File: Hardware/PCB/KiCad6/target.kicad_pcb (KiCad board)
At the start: 2 copper layers, 80 x 82 mm, 70 parts, among them J1 Additional Pins, J2 SW-5V, J3 SW-1, J4 SW-3.3V, J5 SW-2, J6 EXT_LED, J7 Conn_IN, J8 Conn_OUT, J9 USB_B_Micro, Q1 BSS138, Q2 BSS138, Q3 BSS138, Q4 BSS138, Q5 BC817, Q6 BC817, SW1 PROG, SW2 RST, U1 ESP32-WROOM-32D, U2 TSOP312xx, U3 AZ1117-3.3, U4 CH340C

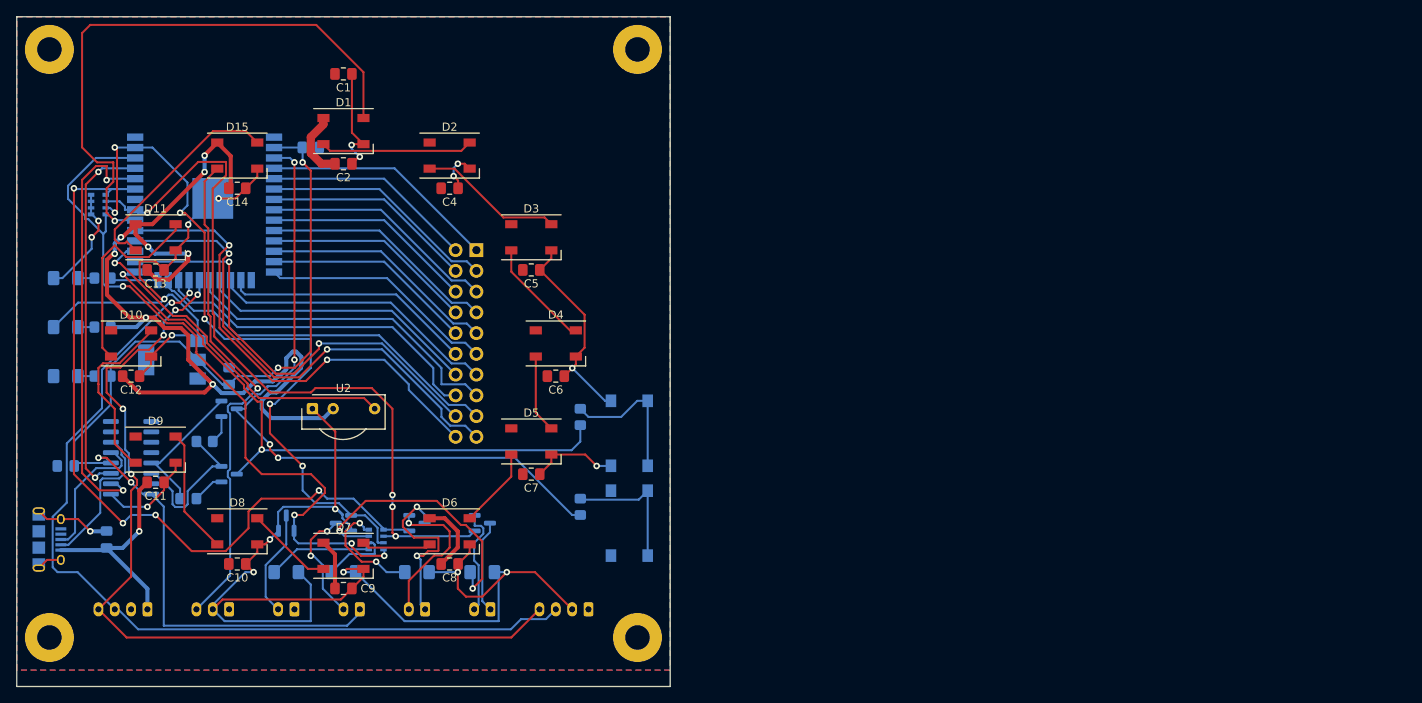
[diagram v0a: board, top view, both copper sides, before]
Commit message: PCB Update from current schema
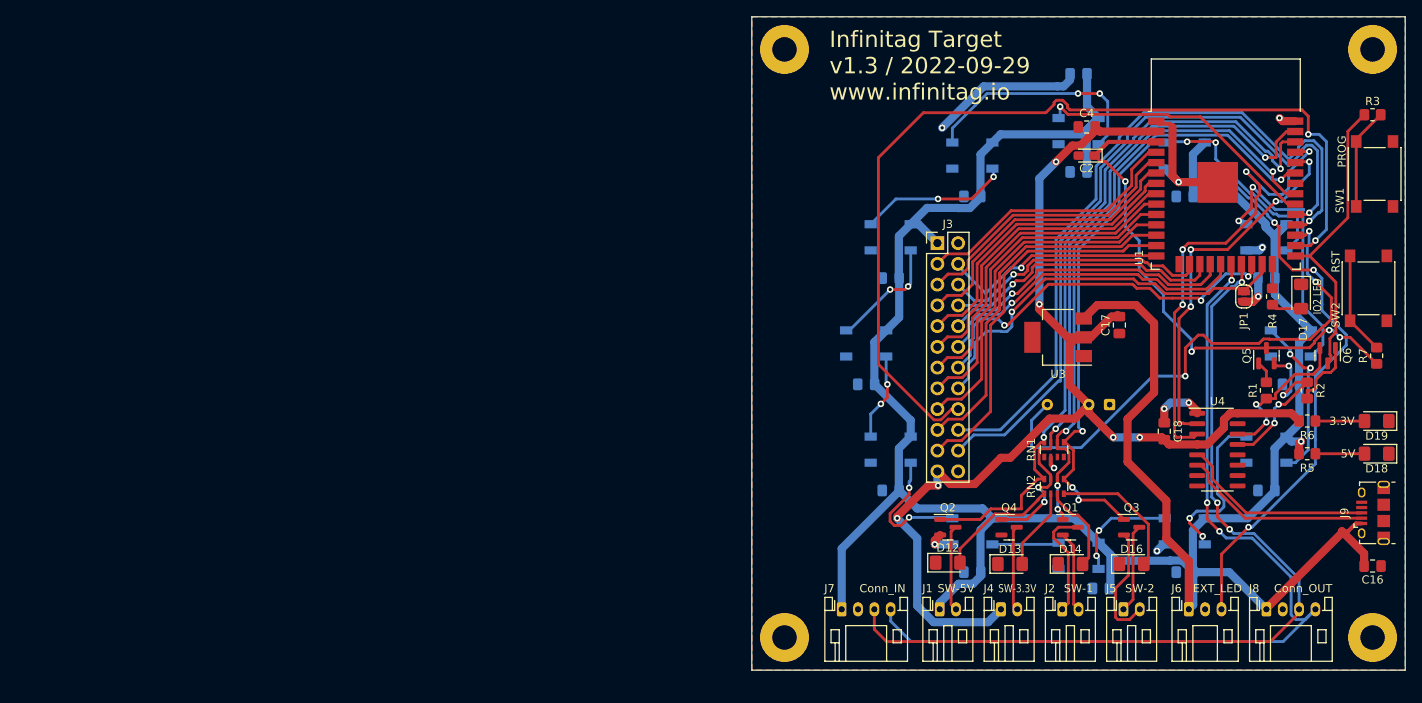
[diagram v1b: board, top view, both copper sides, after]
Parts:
- removed R9: 470, Resistor_SMD:R_0805_2012Metric_Pad1.20x1.40mm_HandSolder
- added C18: 100nF, Capacitor_SMD:C_0805_2012Metric_Pad1.18x1.45mm_HandSolder, F.Cu at (232.5, 100.8)
- added JP1: Disable ESP Log, Jumper:SolderJumper-2_P1.3mm_Open_RoundedPad1.0x1.5mm, F.Cu at (242.2, 84.2)
- added R3: 470, Resistor_SMD:R_0805_2012Metric_Pad1.20x1.40mm_HandSolder, F.Cu at (258.0, 62.0)
- C1: value 100uF -> 100nF; moved to B.Cu
- C10, C11, C12, C13, C14, C5, C6, C7, C8, C9, D1, D10, D11, D15, D2, D3, D4, D5, D6, D7, D8, D9, U2: moved to B.Cu
- C15: value 4.7uF -> 100nF
- C16: value 10uF -> 4.7uF; moved to F.Cu
- C17: value 100nF -> 10uF; moved to F.Cu
- C2: value 100nF -> 10uF; footprint Capacitor_SMD:C_0805_2012Metric_Pad1.18x1.45mm_HandSolder -> Capacitor_Tantalum_SMD:CP_EIA-2012-12_Kemet-R_Pad1.30x1.05mm_HandSolder
- D12, D13, D14, D16, D18, D19, J4, J5, J6, J7, J8, J9, Q1, Q2, Q3, Q4, Q5, Q6, R1, R2, R4, R7, RN1, RN2, SW1, SW2, U1, U3, U4: moved to F.Cu
- D17: value IO2 -> IO2 LED; moved to F.Cu
- J1: value Additional Pins -> SW-5V; footprint Connector_PinHeader_2.54mm:PinHeader_2x10_P2.54mm_Vertical -> Connector_JST:JST_PH_S2B-PH-K_1x02_P2.00mm_Horizontal; moved to F.Cu
- J2: value SW-5V -> SW-1; moved to F.Cu
- J3: value SW-1 -> Conn_02x12_Odd_Even; footprint Connector_JST:JST_PH_S2B-PH-K_1x02_P2.00mm_Horizontal -> Connector_PinHeader_2.54mm:PinHeader_2x12_P2.54mm_Vertical; moved to F.Cu
- R5: value 470 -> 1K; moved to F.Cu
- R6: value 1K -> 470; moved to F.Cu
- moved J9 162.1 mm to (258.1, 110.7)
- moved D18 161.2 mm to (258.5, 103.5), turned to 180 degrees
- moved D19 160.6 mm to (258.5, 99.5), turned to 180 degrees
- moved R7 156.0 mm to (258.5, 91.5), turned to 90 degrees
- moved D17 151.3 mm to (249.2, 84.2), turned to -90 degrees
- moved R5 149.0 mm to (250.0, 103.5), turned to 0 degrees
- moved R6 147.9 mm to (250.0, 99.5), turned to 0 degrees
- moved D10 142.0 mm to (248.0, 90.0), turned to 180 degrees
- moved C16 141.9 mm to (258.0, 117.2), turned to 180 degrees
- moved C12 139.7 mm to (245.0, 108.0), turned to 0 degrees
- moved C13 139.7 mm to (248.0, 95.0), turned to 0 degrees
- moved C15 138.5 mm to (235.0, 72.0), turned to 0 degrees
- moved R2 137.6 mm to (250.0, 95.8), turned to -90 degrees
- moved J8 137.0 mm to (245.0, 122.5), turned to 0 degrees
- moved D11 136.0 mm to (245.0, 77.0), turned to 180 degrees
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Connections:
- C16 pad 2: +3V3 -> +5V
- C2 pad 1: GND -> /ESP_EN
- C2 pad 2: +5V -> GND
- C3 pad 2: +3V3 -> +5V
- C4 pad 2: +5V -> +3V3
- J1 pad 1: /ESP_A_P4 -> +5V
- J1 pad 2: /ESP_A_P5 -> Net-(J1-Pad2)
- J2 pad 1: +5V -> Net-(J2-Pad1)
- J3 pad 1: Net-(J3-Pad1) -> +5V
- J3 pad 2: Net-(J3-Pad2) -> GND
- Q1 pad 2: Net-(J3-Pad2) -> Net-(J2-Pad2)
- Q1 pad 3: Net-(J3-Pad1) -> Net-(J2-Pad1)
- Q2 pad 3: Net-(J2-Pad2) -> Net-(J1-Pad2)
- R4 pad 1: /ESP_IO0 -> /ESP_IO2
- R4 pad 2: Net-(R4-Pad2) -> Net-(D17-Pad2)
- R5 pad 1: /ESP_IO2 -> +5V
- R5 pad 2: Net-(D17-Pad2) -> Net-(D18-Pad2)
- R6 pad 1: +5V -> +3V3
- R6 pad 2: Net-(D18-Pad2) -> Net-(D19-Pad2)
- R7 pad 1: +3V3 -> /ESP_EN
- R7 pad 2: Net-(D19-Pad2) -> Net-(R7-Pad2)
- SW1 pad 1: Net-(R4-Pad2) -> Net-(R3-Pad2)
- SW2 pad 1: Net-(R9-Pad2) -> Net-(R7-Pad2)
- U2 pad 2: +5V -> +3V3
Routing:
- net GND: track 297.3 -> 57.0 mm, vias 20 -> 10
- net +5V: track 169.7 -> 332.7 mm, vias 9 -> 1
- net /ESP_A_P26: track 55.2 -> 115.3 mm
- net /ESP_IO0: track 77.5 -> 36.8 mm, vias 2 -> 0
- net /LED_DIN: track 71.9 -> 35.2 mm
- net /ESP_A_P29: track 59.9 -> 87.5 mm, vias 2 -> 1
- net /ESP_A_P28: track 61.4 -> 88.5 mm, vias 2 -> 1
- net /IR_RCV: track 43.0 -> 66.2 mm, vias 1 -> 3
- net Net-(D14-Pad2): track 33.6 -> 10.9 mm, vias 2 -> 0
- net /ESP_EN: track 85.3 -> 63.1 mm
- net /SW_2: track 98.6 -> 78.4 mm
- net /ESP_A_P13: track 25.9 -> 46.0 mm
- net Net-(R4-Pad2): track 17.4 -> 0.00 mm
- net /SW_1: track 93.4 -> 76.0 mm
- net /ESP_A_P11: track 25.9 -> 42.9 mm
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- added copper zone on F.Cu, net GND
- removed copper zone on F.Cu, net +5V
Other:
- board size 80 x 82 mm -> 80 x 80 mm
- board text added: "Infinitag Target v1.3 / 2022-09-29 www.infinitag.io"
- board text removed: "Infinitag Target v1.2 / 2022-09-06 www.infinitag.io"

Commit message: PCB files with current changes updated
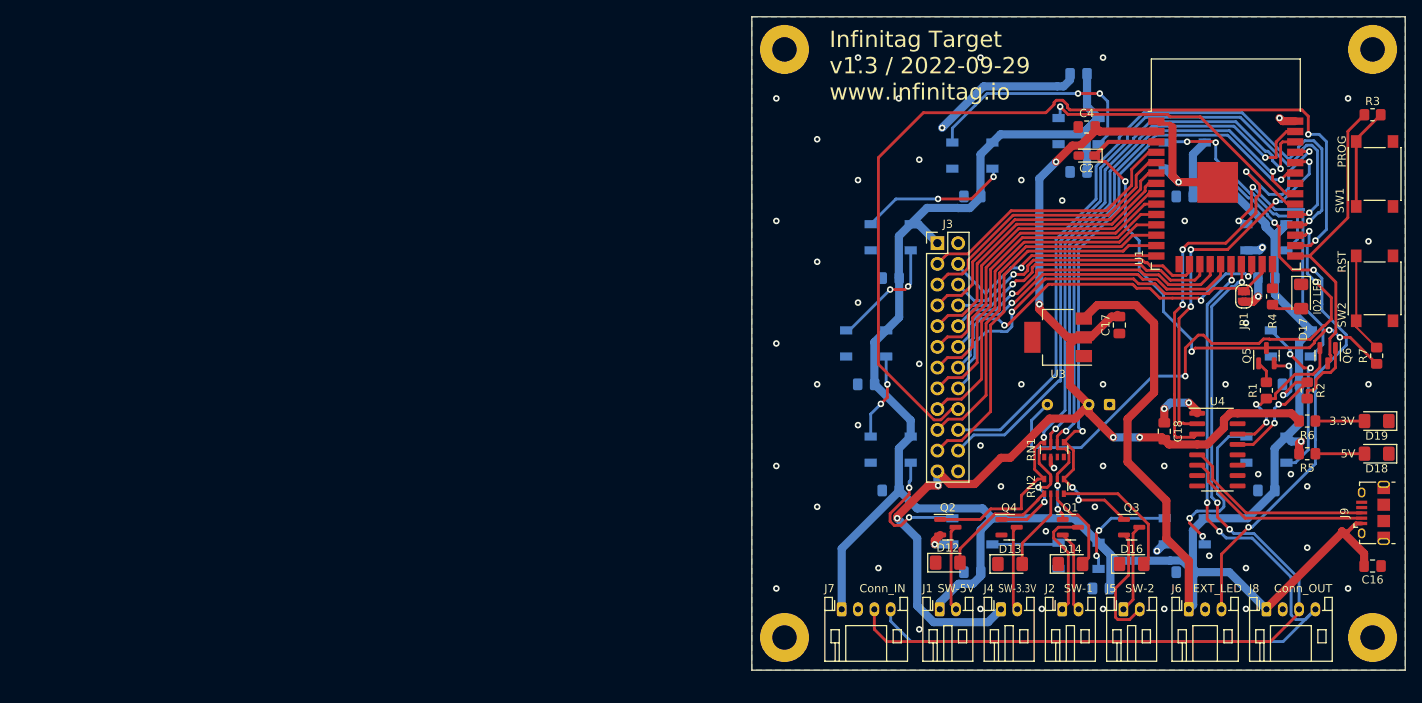
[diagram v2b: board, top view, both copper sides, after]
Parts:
- moved SW2 0.75 mm to (258.2, 83.2)
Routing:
- net GND: vias 10 -> 58
